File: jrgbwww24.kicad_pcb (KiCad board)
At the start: 2 copper layers, 85 x 56 mm, 33 parts, among them J1 Srew_terminal, J2 Screw_Terminal_01x06, Q1 2N3904, Q10 IPA040N06N, Q2 2N3904, Q3 2N3904, Q4 IPA040N06N, Q5 IPA040N06N, Q6 IPA040N06N, Q7 2N3904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

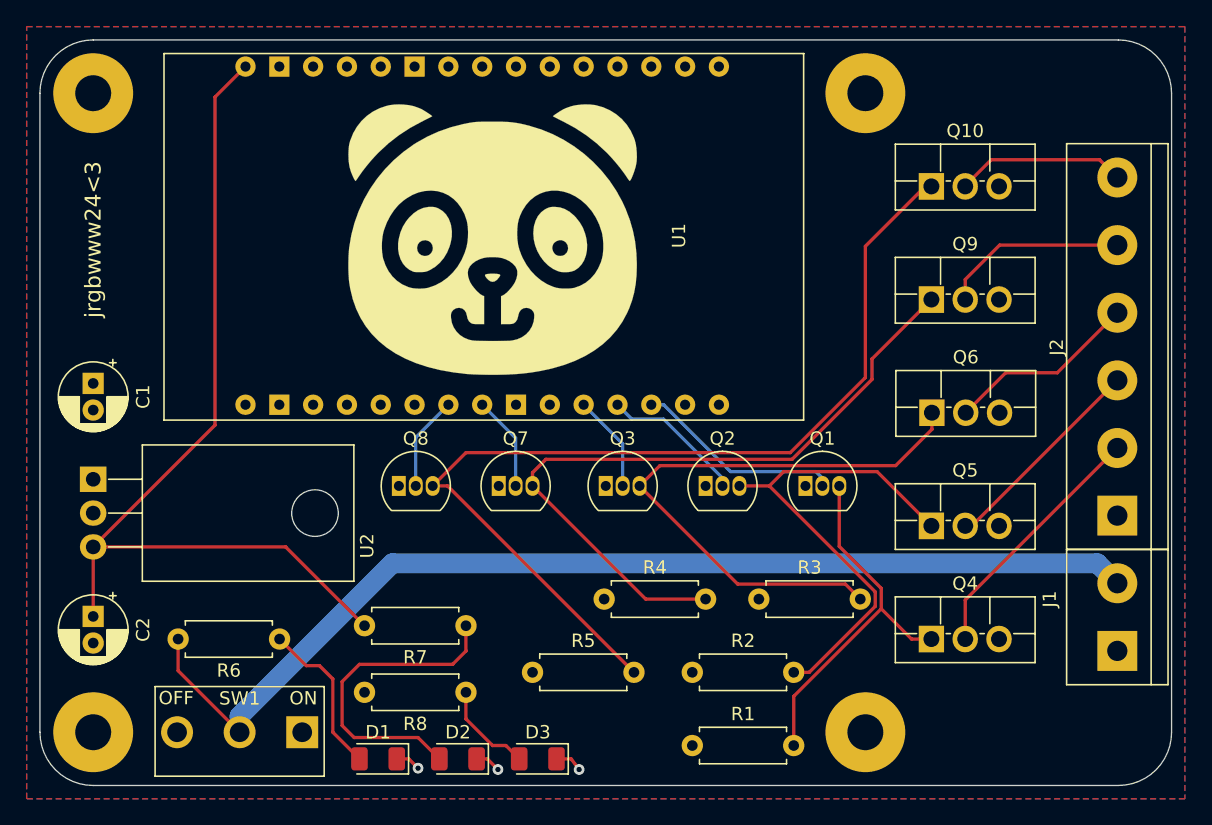
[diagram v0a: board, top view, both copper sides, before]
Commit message: fixed footprints, schematics
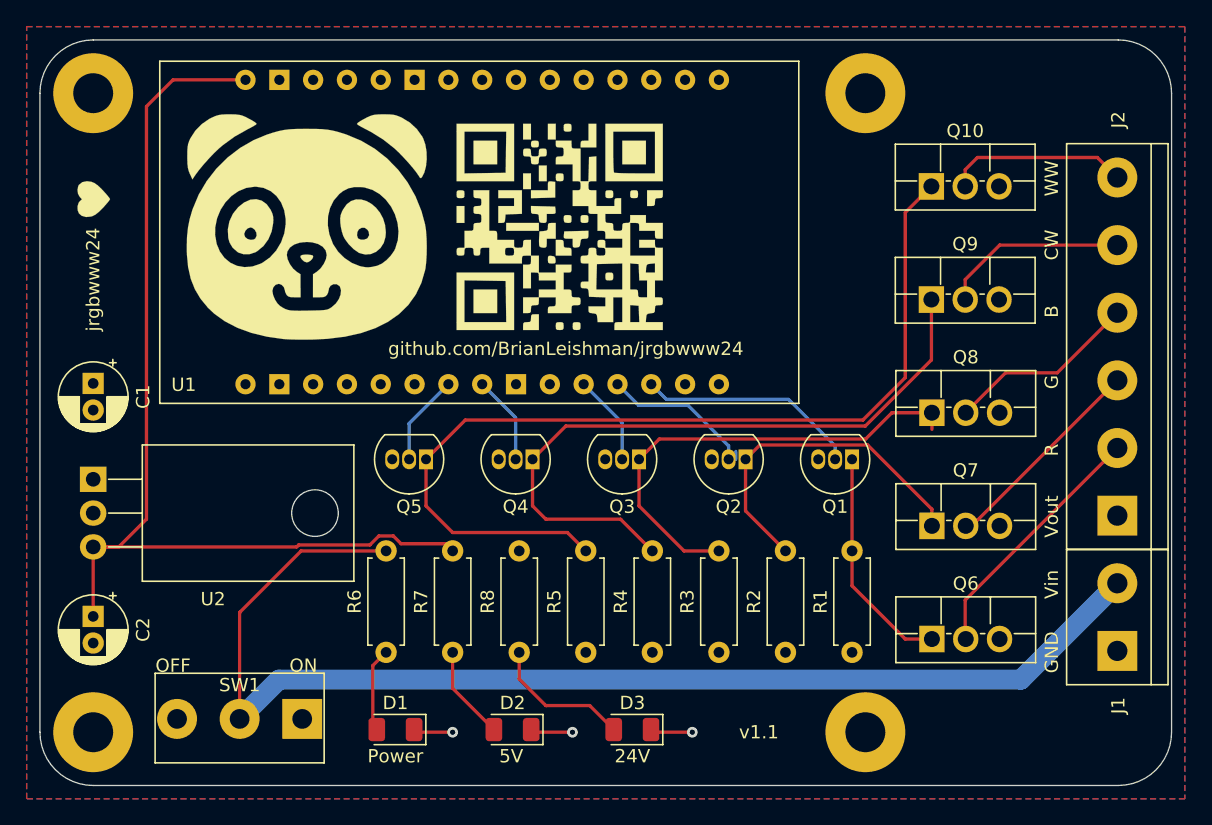
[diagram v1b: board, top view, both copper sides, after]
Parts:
- added G***: LOGO, jrgbwww24:qr, F.Cu at (129.0, 74.0)
- added G***: LOGO, jrgbwww24:heart, F.Cu at (94.0, 72.0)
- D1: value RED - ALWAY ON -> RED - ALWAYS ON
- D2: value YELLOW - 5V -> GREEN - 5V
- Q4, Q5: value IPA040N06N -> 2N3904; footprint Package_TO_SOT_THT:TO-220F-3_Vertical -> Package_TO_SOT_THT:TO-92_Inline
- Q7, Q8: value 2N3904 -> IPA040N06N; footprint Package_TO_SOT_THT:TO-92_Inline -> Package_TO_SOT_THT:TO-220F-3_Vertical
- R7: value 125 -> 100
- moved Q8 40.4 mm to (157.0, 88.0)
- moved Q5 38.3 mm to (119.0, 91.5), turned to 180 degrees
- moved Q4 32.9 mm to (127.0, 91.5), turned to 180 degrees
- moved Q7 32.7 mm to (157.0, 96.5)
- moved Q6 17.0 mm to (157.0, 105.0)
- moved G*** 14.0 mm to (110.0, 74.0)
- moved R1 13.9 mm to (151.0, 106.0), turned to 90 degrees
- moved R6 8.06 mm to (116.0, 106.0), turned to 90 degrees
- moved D3 7.43 mm to (134.5, 111.8)
- moved R2 7.16 mm to (146.0, 106.0), turned to 90 degrees
- moved R4 5.39 mm to (136.0, 106.0), turned to 90 degrees
- moved R3 5.00 mm to (141.0, 106.0), turned to 90 degrees
- moved R8 5.00 mm to (126.0, 106.0), turned to 90 degrees
- moved D2 4.65 mm to (125.5, 111.8)
- moved R5 4.27 mm to (131.0, 106.0), turned to 90 degrees
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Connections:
- C1 pad 1: Earth -> +24V
- C1 pad 2: +24V -> Earth
- Q1 pad 1: Earth -> Net-(Q1-Pad1)
- Q1 pad 3: Net-(Q1-Pad3) -> Earth
- Q2 pad 1: Earth -> Net-(Q2-Pad1)
- Q2 pad 3: Net-(Q2-Pad3) -> Earth
- Q3 pad 1: Earth -> Net-(Q3-Pad1)
- Q3 pad 3: Net-(Q3-Pad3) -> Earth
- Q4 pad 1: Net-(Q1-Pad3) -> Net-(Q4-Pad1)
- Q4 pad 2: /R_GND -> /CW_SIGNAL
- Q5 pad 1: Net-(Q2-Pad3) -> Net-(Q10-Pad1)
- Q5 pad 2: /G_GND -> /WW_SIGNAL
- Q6 pad 1: Net-(Q3-Pad3) -> Net-(Q1-Pad1)
- Q6 pad 2: /B_GND -> /R_GND
- Q7 pad 1: Earth -> Net-(Q2-Pad1)
- Q7 pad 2: /CW_SIGNAL -> /G_GND
- Q7 pad 3: Net-(Q7-Pad3) -> Earth
- Q8 pad 1: Earth -> Net-(Q3-Pad1)
- Q8 pad 2: /WW_SIGNAL -> /B_GND
- Q8 pad 3: Net-(Q10-Pad1) -> Earth
- Q9 pad 1: Net-(Q7-Pad3) -> Net-(Q4-Pad1)
- R1 pad 2: Net-(Q1-Pad3) -> Net-(Q1-Pad1)
- R2 pad 2: Net-(Q2-Pad3) -> Net-(Q2-Pad1)
- R3 pad 2: Net-(Q3-Pad3) -> Net-(Q3-Pad1)
- R4 pad 2: Net-(Q7-Pad3) -> Net-(Q4-Pad1)
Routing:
- net Net-(Q7-Pad3): track 53.8 -> 0.00 mm
- net Net-(Q4-Pad1): track 0.00 -> 51.5 mm
- net Net-(Q3-Pad3): track 45.1 -> 0.00 mm
- net Net-(Q2-Pad3): track 37.1 -> 0.00 mm
- net Net-(Q3-Pad1): track 0.00 -> 35.6 mm
- net Net-(Q1-Pad3): track 28.7 -> 0.00 mm
- net Net-(Q2-Pad1): track 0.00 -> 25.8 mm
- net Net-(Q1-Pad1): track 0.00 -> 17.6 mm
- net Net-(D2-Pad2): track 23.8 -> 7.08 mm
- net VDD: track 81.4 -> 91.1 mm
- net +5V: track 68.9 -> 77.2 mm
- net Net-(D1-Pad2): track 12.1 -> 6.34 mm
- net Net-(D3-Pad2): track 7.24 -> 10.7 mm
- net Earth: track 5.92 -> 9.35 mm
- net Net-(Q10-Pad1): track 73.5 -> 70.6 mm
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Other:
- board text added: "24V"
- board text added: "5V"
- board text added: "B"
- board text added: "CW"
- board text added: "G"
- board text added: "GND"
- board text added: "Power"
- board text added: "R"
- board text added: "Vin"
- board text added: "Vout"
- board text added: "WW"
- board text added: "github.com/BrianLeishman/jrgbwww24"
- board text added: "jrgbwww24"
- board text added: "v1.1"
- board text removed: "jrgbwww24<3"

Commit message: improved 5v, fan header
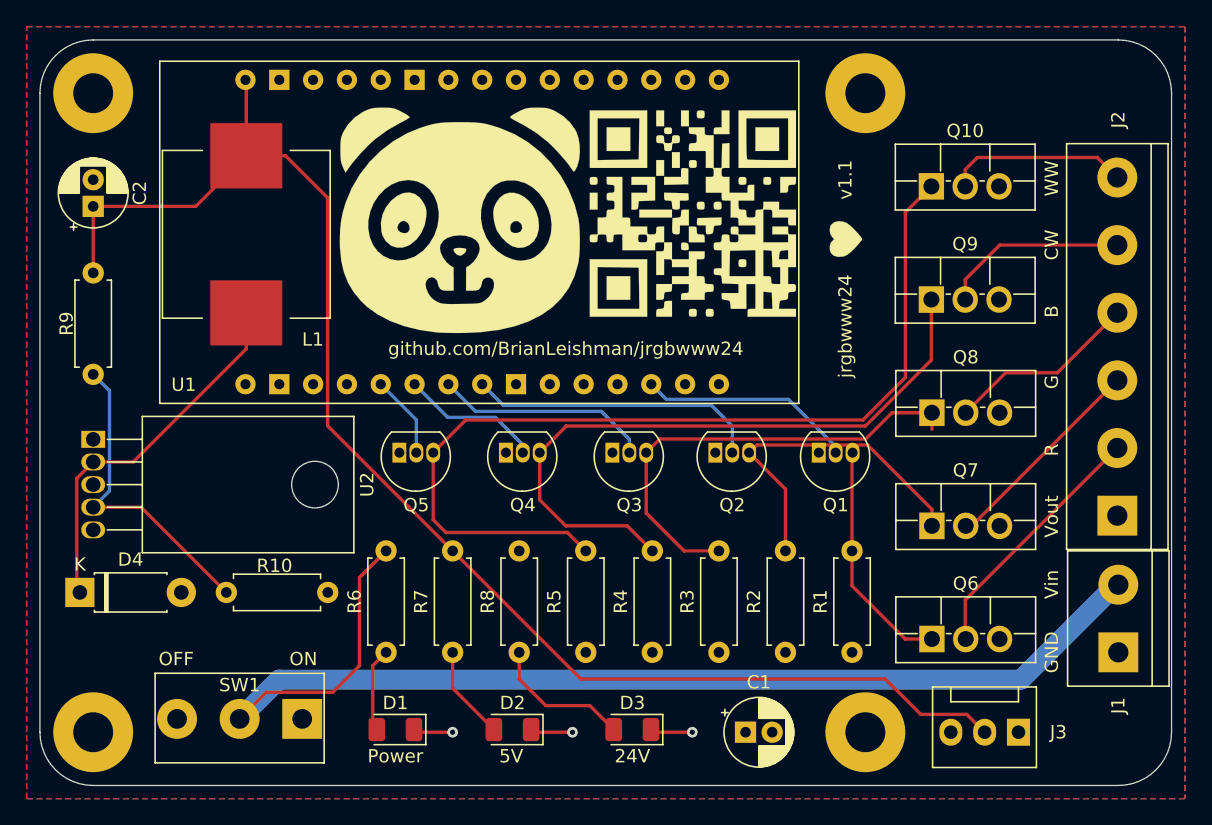
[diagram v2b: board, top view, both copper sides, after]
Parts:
- added D4: SB160-E3/73, Diode_THT:D_DO-41_SOD81_P7.62mm_Horizontal, F.Cu at (93.0, 101.5)
- added J3: Fan, Connector:FanPinHeader_1x03_P2.54mm_Vertical, F.Cu at (163.5, 112.0)
- added L1: 330u, Inductor_SMD:L_Wuerth_WE-PD-Typ-LS_Handsoldering, F.Cu at (105.5, 74.6)
- added R10: 2k, Resistor_THT:R_Axial_DIN0207_L6.3mm_D2.5mm_P7.62mm_Horizontal, F.Cu at (104.0, 101.5)
- added R9: 6.12k, Resistor_THT:R_Axial_DIN0207_L6.3mm_D2.5mm_P7.62mm_Horizontal, F.Cu at (94.0, 77.5)
- C1: value 0.33u -> 100u
- C2: value 0.1u -> 330u
- Q1, Q2, Q3, Q4, Q5: footprint Package_TO_SOT_THT:TO-92_Inline -> jrgbwww24:TO-92_Inline
- U2: value L7805 -> TL2575; footprint Package_TO_SOT_THT:TO-220-3_Horizontal_TabDown -> Package_TO_SOT_THT:TO-220-5_Horizontal_TabDown
- moved G*** 56.6 mm to (150.5, 75.0)
- moved C1 55.6 mm to (143.0, 112.0), turned to 0 degrees
- moved C2 30.8 mm to (94.0, 72.5), turned to 90 degrees
- moved G*** 11.5 mm to (121.5, 73.5)
- moved G*** 10.0 mm to (139.0, 73.0)
- moved U2 3.00 mm to (94.0, 90.0)
- moved Q1 2.55 mm to (148.5, 92.0), turned to 0 degrees
- moved Q2 2.32 mm to (140.7, 92.0), turned to 0 degrees
- moved Q3 2.06 mm to (133.0, 92.0), turned to 0 degrees
- moved Q4 2.06 mm to (125.0, 92.0), turned to 0 degrees
- moved Q5 2.06 mm to (117.0, 92.0), turned to 0 degrees
- moved J1 0.13 mm to (171.0, 106.0)
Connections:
- Q1 pad 1: Net-(Q1-Pad1) -> Earth
- Q1 pad 3: Earth -> Net-(Q1-Pad3)
- Q2 pad 1: Net-(Q2-Pad1) -> Earth
- Q2 pad 3: Earth -> Net-(Q2-Pad3)
- Q3 pad 1: Net-(Q3-Pad1) -> Earth
- Q3 pad 3: Earth -> Net-(Q3-Pad3)
- Q4 pad 1: Net-(Q4-Pad1) -> Earth
- Q4 pad 3: Earth -> Net-(Q4-Pad3)
- Q5 pad 1: Net-(Q10-Pad1) -> Earth
- Q5 pad 3: Earth -> Net-(Q10-Pad1)
- Q6 pad 1: Net-(Q1-Pad1) -> Net-(Q1-Pad3)
- Q7 pad 1: Net-(Q2-Pad1) -> Net-(Q2-Pad3)
- Q8 pad 1: Net-(Q3-Pad1) -> Net-(Q3-Pad3)
- Q9 pad 1: Net-(Q4-Pad1) -> Net-(Q4-Pad3)
- R1 pad 2: Net-(Q1-Pad1) -> Net-(Q1-Pad3)
- R2 pad 2: Net-(Q2-Pad1) -> Net-(Q2-Pad3)
- R3 pad 2: Net-(Q3-Pad1) -> Net-(Q3-Pad3)
- R4 pad 2: Net-(Q4-Pad1) -> Net-(Q4-Pad3)
- U1 pad 19: /G_SIGNAL -> Net-(U1-Pad19)
- U1 pad 20: /B_SIGNAL -> Net-(U1-Pad20)
- U1 pad 23: /CW_SIGNAL -> /G_SIGNAL
- U1 pad 24: /WW_SIGNAL -> /B_SIGNAL
- U1 pad 25: Net-(U1-Pad25) -> /CW_SIGNAL
- U1 pad 26: Net-(U1-Pad26) -> /WW_SIGNAL
- U2 pad 2: Earth -> Net-(D4-Pad1)
- U2 pad 3: +5V -> Earth
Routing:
- net Net-(Q4-Pad1): track 51.5 -> 0.00 mm
- net Net-(Q4-Pad3): track 0.00 -> 50.5 mm
- net Net-(Q3-Pad1): track 35.6 -> 0.00 mm
- net Net-(Q3-Pad3): track 0.00 -> 35.2 mm
- net +5V: track 77.2 -> 110.5 mm
- net Net-(D4-Pad1): track 0.00 -> 28.1 mm
- net Net-(Q2-Pad1): track 25.8 -> 0.00 mm
- net Net-(Q2-Pad3): track 0.00 -> 25.7 mm
- net Net-(R10-Pad1): track 0.00 -> 23.6 mm
- net Net-(Q1-Pad3): track 0.00 -> 17.6 mm
- net Net-(Q1-Pad1): track 17.6 -> 0.00 mm
- net /G_SIGNAL: track 11.9 -> 22.1 mm
- net /B_SIGNAL: track 6.84 -> 16.3 mm
- net /CW_SIGNAL: track 6.68 -> 10.6 mm
- net VDD: track 91.1 -> 90.3 mm
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
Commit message: fixed 5 v power supply
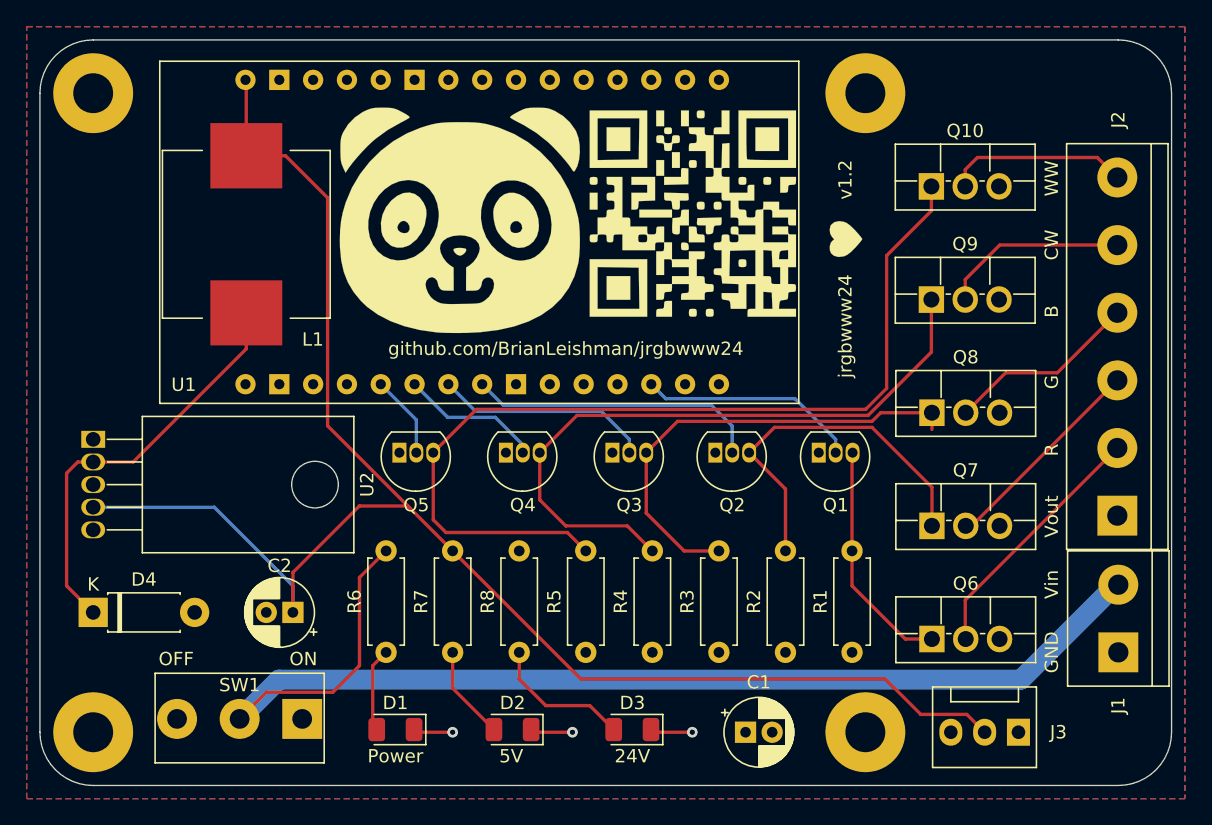
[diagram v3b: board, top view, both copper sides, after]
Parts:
- removed R10: 2k, Resistor_THT:R_Axial_DIN0207_L6.3mm_D2.5mm_P7.62mm_Horizontal
- removed R9: 6.12k, Resistor_THT:R_Axial_DIN0207_L6.3mm_D2.5mm_P7.62mm_Horizontal
- moved C2 34.0 mm to (109.0, 103.0), turned to 180 degrees
- moved D4 1.80 mm to (94.0, 103.0)
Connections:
- U2 pad 4: Net-(R10-Pad1) -> +5V
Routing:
- net Net-(R10-Pad1): track 23.6 -> 0.00 mm
- net +5V: track 110.5 -> 125.9 mm
- net Net-(D4-Pad1): track 28.1 -> 31.4 mm
- net Net-(Q2-Pad3): track 25.7 -> 27.8 mm
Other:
- board text added: "v1.2"
- board text removed: "v1.1"
